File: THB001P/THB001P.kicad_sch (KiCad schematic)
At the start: 3 parts, among them J1 Conn_01x03, J2 Conn_01x03, U1 THB001P

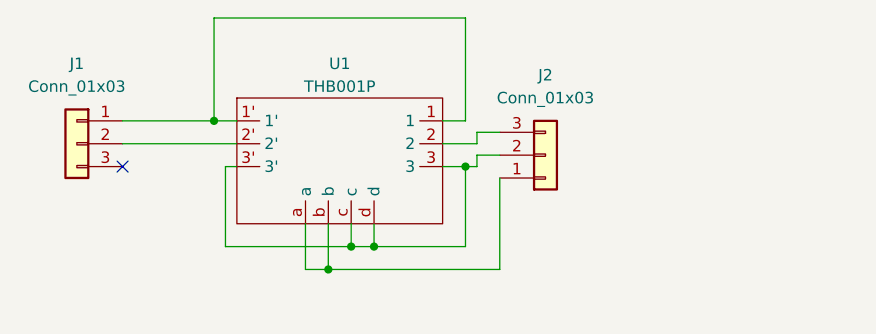
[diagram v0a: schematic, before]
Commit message: Starting work on Thumbstick (THB001P)
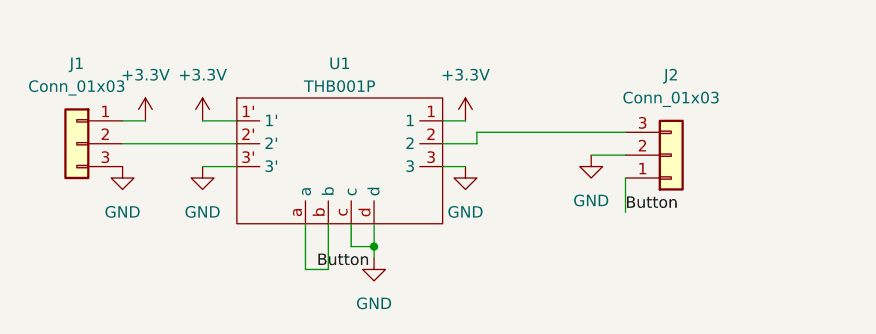
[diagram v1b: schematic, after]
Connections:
- net Button: now reaches J2.1 (Pin_1), U1.a, U1.b
- net GND: now reaches J2.2 (Pin_2), U1.3, U1.3', U1.c, U1.d
- net GND: now also J1.3 (Pin_3)
- net +3V3: now reaches J1.1 (Pin_1), U1.1, U1.1'
- no-connect marks 1 -> 0
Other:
- moved on the sheet: J2

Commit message: Generating gerbers for board
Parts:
- removed J1, J2: Conn_01x03, Connector_PinHeader_2.54mm:PinHeader_1x03_P2.54mm_Vertical, symbol Connector_Generic:Conn_01x03
- added J1: Conn_01x05, Connector_PinHeader_2.54mm:PinHeader_1x05_P2.54mm_Vertical, symbol Connector_Generic:Conn_01x05
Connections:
- net +3V3: now also J1.2 (Pin_2)
- net Button: now also J1.5 (Pin_5)
- net GND: now also J1.1 (Pin_1)
- net 2: now reaches U1.2
- net 2: now also J1.3 (Pin_3)
- net 2': now reaches U1.2'
- net 2': now also J1.4 (Pin_4)
